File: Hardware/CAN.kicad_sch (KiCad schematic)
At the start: 10 parts, among them J4 Conn_01x02_Pin, U6 TCAN337, U7 CDSOT23-T24CAN

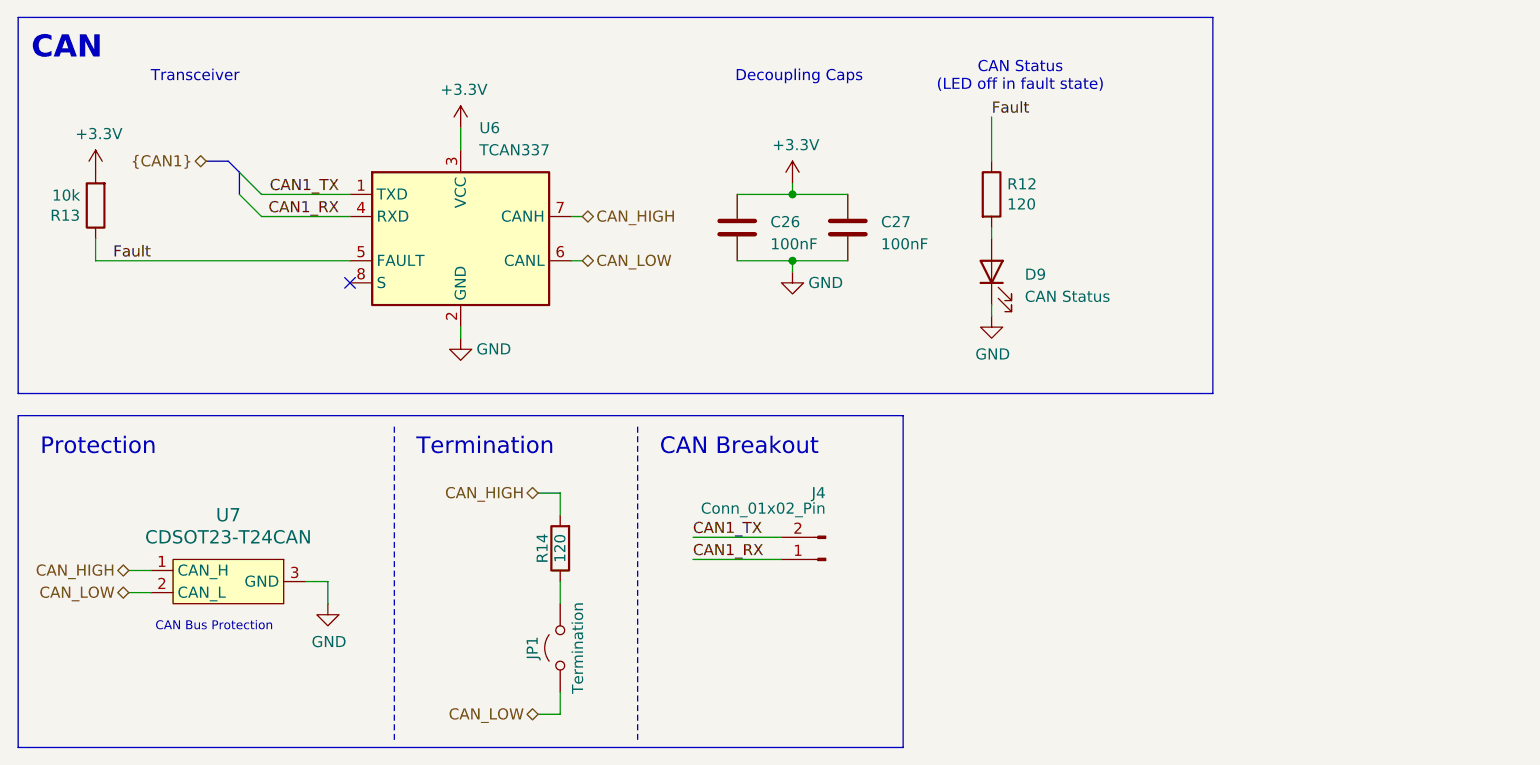
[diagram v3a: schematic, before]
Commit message: changed to 2 channel op amp, stole RPP from PSOM
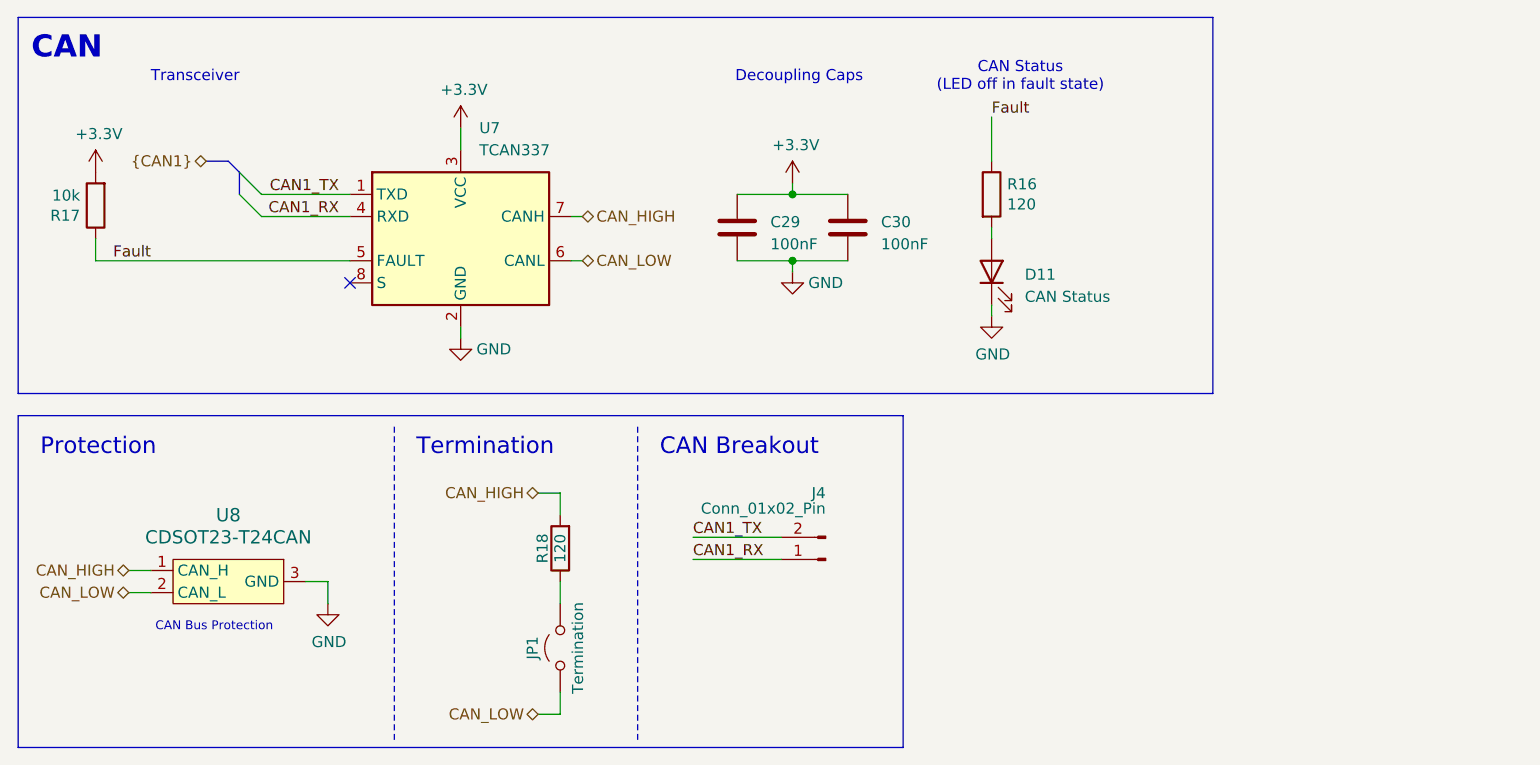
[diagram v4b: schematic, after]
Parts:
- renumbered C26 to C29, C27 to C30, D9 to D11, R12 to R16, R13 to R17, R14 to R18, U6 to U7, U7 to U8
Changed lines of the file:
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@@
 		(on_board yes)
 		(dnp no)
-		(property "Reference" "#PWR062"
+		(property "Reference" "#PWR078"
 			(at 50.8 88.9 0)
 			(effects
@@
 			(project "BPS-AmperesPCB"
 				(path "/a452d214-ea00-440d-a445-5d6103fda43a/2dff07b6-7dab-4ebe-8bad-c03f5c351937"
-					(reference "#PWR062")
+					(reference "#PWR078")
 					(unit 1)
 				)
@@
 		(on_board yes)
 		(dnp no)
-		(property "Reference" "C26"
+		(property "Reference" "C29"
 			(at 101.6 38.735 0)
 			(effects
@@
 			(project "BPS-AmperesPCB"
 				(path "/a452d214-ea00-440d-a445-5d6103fda43a/2dff07b6-7dab-4ebe-8bad-c03f5c351937"
-					(reference "C26")
+					(reference "C29")
 					(unit 1)
 				)
@@
 		(on_board yes)
 		(dnp no)
-		(property "Reference" "R13"
+		(property "Reference" "R17"
 			(at 22.352 37.9984 0)
 			(effects
@@
 			(project "BPS-AmperesPCB"
 				(path "/a452d214-ea00-440d-a445-5d6103fda43a/2dff07b6-7dab-4ebe-8bad-c03f5c351937"
-					(reference "R13")
+					(reference "R17")
 					(unit 1)
 				)
@@
 		(on_board yes)
 		(dnp no)
-		(property "Reference" "R14"
+		(property "Reference" "R18"
 			(at 75.438 76.2 90)
 			(effects
@@
 			(project "BPS-AmperesPCB"
 				(path "/a452d214-ea00-440d-a445-5d6103fda43a/2dff07b6-7dab-4ebe-8bad-c03f5c351937"
-					(reference "R14")
+					(reference "R18")
 					(unit 1)
 				)
@@
 		(on_board yes)
 		(dnp no)
-		(property "Reference" "#PWR060"
+		(property "Reference" "#PWR076"
 			(at 127 55.88 0)
 			(effects
@@
 			(project "BPS-AmperesPCB"
 				(path "/a452d214-ea00-440d-a445-5d6103fda43a/2dff07b6-7dab-4ebe-8bad-c03f5c351937"
-					(reference "#PWR060")
+					(reference "#PWR076")
 					(unit 1)
 				)
@@
 		(on_board yes)
 		(dnp no)
-		(property "Reference" "U7"
+		(property "Reference" "U8"
 			(at 39.37 72.39 0)
 			(effects
@@
 			(project "BPS-AmperesPCB"
 				(path "/a452d214-ea00-440d-a445-5d6103fda43a/2dff07b6-7dab-4ebe-8bad-c03f5c351937"
-					(reference "U7")
+					(reference "U8")
 					(unit 1)
 				)
@@
 		(dnp no)
 		(fields_autoplaced yes)
-		(property "Reference" "D9"
+		(property "Reference" "D11"
 			(at 130.81 44.7674 90)
 			(effects
@@
 			(project ""
 				(path "/a452d214-ea00-440d-a445-5d6103fda43a/2dff07b6-7dab-4ebe-8bad-c03f5c351937"
-					(reference "D9")
+					(reference "D11")
 					(unit 1)
 				)
@@
 		(on_board yes)
 		(dnp no)
-		(property "Reference" "#PWR057"
+		(property "Reference" "#PWR073"
 			(at 24.13 36.83 0)
 			(effects
@@
 			(project "BPS-AmperesPCB"
 				(path "/a452d214-ea00-440d-a445-5d6103fda43a/2dff07b6-7dab-4ebe-8bad-c03f5c351937"
-					(reference "#PWR057")
+					(reference "#PWR073")
 					(unit 1)
 				)
@@
 		(dnp no)
 		(fields_autoplaced yes)
-		(property "Reference" "C27"
+		(property "Reference" "C30"
 			(at 114.3 38.735 0)
 			(effects
@@
 			(project "BPS-AmperesPCB"
 				(path "/a452d214-ea00-440d-a445-5d6103fda43a/2dff07b6-7dab-4ebe-8bad-c03f5c351937"
-					(reference "C27")
+					(reference "C30")
 					(unit 1)
 				)
@@
 		(dnp no)
 		(fields_autoplaced yes)
-		(property "Reference" "U6"
+		(property "Reference" "U7"
 			(at 68.1833 27.94 0)
 			(effects
@@
 			(project "BPS-AmperesPCB"
 				(path "/a452d214-ea00-440d-a445-5d6103fda43a/2dff07b6-7dab-4ebe-8bad-c03f5c351937"
-					(reference "U6")
+					(reference "U7")
 					(unit 1)
 				)
@@
 		(on_board yes)
 		(dnp no)
-		(property "Reference" "#PWR056"
+		(property "Reference" "#PWR072"
 			(at 66.04 31.75 0)
 			(effects
@@
 			(project "BPS-AmperesPCB"
 				(path "/a452d214-ea00-440d-a445-5d6103fda43a/2dff07b6-7dab-4ebe-8bad-c03f5c351937"
-					(reference "#PWR056")
+					(reference "#PWR072")
 					(unit 1)
 				)
@@
 		(on_board yes)
 		(dnp no)
-		(property "Reference" "#PWR059"
+		(property "Reference" "#PWR075"
 			(at 104.14 50.8 0)
 			(effects
@@
 			(project "BPS-AmperesPCB"
 				(path "/a452d214-ea00-440d-a445-5d6103fda43a/2dff07b6-7dab-4ebe-8bad-c03f5c351937"
-					(reference "#PWR059")
+					(reference "#PWR075")
 					(unit 1)
 				)
@@
 		(on_board yes)
 		(dnp no)
-		(property "Reference" "#PWR061"
+		(property "Reference" "#PWR077"
 			(at 66.04 58.42 0)
 			(effects
@@
 			(project "BPS-AmperesPCB"
 				(path "/a452d214-ea00-440d-a445-5d6103fda43a/2dff07b6-7dab-4ebe-8bad-c03f5c351937"
-					(reference "#PWR061")
+					(reference "#PWR077")
 					(unit 1)
 				)
@@
 		(on_board yes)
 		(dnp no)
-		(property "Reference" "#PWR058"
+		(property "Reference" "#PWR074"
 			(at 104.14 38.1 0)
 			(effects
@@
 			(project "BPS-AmperesPCB"
 				(path "/a452d214-ea00-440d-a445-5d6103fda43a/2dff07b6-7dab-4ebe-8bad-c03f5c351937"
-					(reference "#PWR058")
+					(reference "#PWR074")
 					(unit 1)
 				)
@@
 		(on_board yes)
 		(dnp no)
-		(property "Reference" "R12"
+		(property "Reference" "R16"
 			(at 128.778 34.3916 0)
 			(effects
@@
 			(project "BPS-AmperesPCB"
 				(path "/a452d214-ea00-440d-a445-5d6103fda43a/2dff07b6-7dab-4ebe-8bad-c03f5c351937"
-					(reference "R12")
-					(unit 1)
-				)
+					(reference "R16")
+					(unit 1)
+				)

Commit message: lay out lay out
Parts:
- renumbered C29 to C30, C30 to C31, D11 to D12, U7 to U6, U8 to U7
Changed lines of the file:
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@@
 		(on_board yes)
 		(dnp no)
-		(property "Reference" "#PWR079"
+		(property "Reference" "#PWR081"
 			(at 50.8 88.9 0)
 			(effects
@@
 			(project "BPS-AmperesPCB"
 				(path "/a452d214-ea00-440d-a445-5d6103fda43a/2dff07b6-7dab-4ebe-8bad-c03f5c351937"
-					(reference "#PWR079")
+					(reference "#PWR081")
 					(unit 1)
 				)
@@
 		(on_board yes)
 		(dnp no)
-		(property "Reference" "C29"
+		(property "Reference" "C30"
 			(at 101.6 38.735 0)
 			(effects
@@
 			(project "BPS-AmperesPCB"
 				(path "/a452d214-ea00-440d-a445-5d6103fda43a/2dff07b6-7dab-4ebe-8bad-c03f5c351937"
-					(reference "C29")
+					(reference "C30")
 					(unit 1)
 				)
@@
 		(on_board yes)
 		(dnp no)
-		(property "Reference" "#PWR077"
+		(property "Reference" "#PWR079"
 			(at 127 55.88 0)
 			(effects
@@
 			(project "BPS-AmperesPCB"
 				(path "/a452d214-ea00-440d-a445-5d6103fda43a/2dff07b6-7dab-4ebe-8bad-c03f5c351937"
-					(reference "#PWR077")
+					(reference "#PWR079")
 					(unit 1)
 				)
@@
 		(on_board yes)
 		(dnp no)
-		(property "Reference" "U8"
+		(property "Reference" "U7"
 			(at 39.37 72.39 0)
 			(effects
@@
 			(project "BPS-AmperesPCB"
 				(path "/a452d214-ea00-440d-a445-5d6103fda43a/2dff07b6-7dab-4ebe-8bad-c03f5c351937"
-					(reference "U8")
+					(reference "U7")
 					(unit 1)
 				)
@@
 		(dnp no)
 		(fields_autoplaced yes)
-		(property "Reference" "D11"
+		(property "Reference" "D12"
 			(at 130.81 44.7674 90)
 			(effects
@@
 			(project ""
 				(path "/a452d214-ea00-440d-a445-5d6103fda43a/2dff07b6-7dab-4ebe-8bad-c03f5c351937"
-					(reference "D11")
+					(reference "D12")
 					(unit 1)
 				)
@@
 		(on_board yes)
 		(dnp no)
-		(property "Reference" "#PWR074"
+		(property "Reference" "#PWR076"
 			(at 24.13 36.83 0)
 			(effects
@@
 			(project "BPS-AmperesPCB"
 				(path "/a452d214-ea00-440d-a445-5d6103fda43a/2dff07b6-7dab-4ebe-8bad-c03f5c351937"
-					(reference "#PWR074")
+					(reference "#PWR076")
 					(unit 1)
 				)
@@
 		(dnp no)
 		(fields_autoplaced yes)
-		(property "Reference" "C30"
+		(property "Reference" "C31"
 			(at 114.3 38.735 0)
 			(effects
@@
 			(project "BPS-AmperesPCB"
 				(path "/a452d214-ea00-440d-a445-5d6103fda43a/2dff07b6-7dab-4ebe-8bad-c03f5c351937"
-					(reference "C30")
+					(reference "C31")
 					(unit 1)
 				)
@@
 		(dnp no)
 		(fields_autoplaced yes)
-		(property "Reference" "U7"
+		(property "Reference" "U6"
 			(at 68.1833 27.94 0)
 			(effects
@@
 			(project "BPS-AmperesPCB"
 				(path "/a452d214-ea00-440d-a445-5d6103fda43a/2dff07b6-7dab-4ebe-8bad-c03f5c351937"
-					(reference "U7")
+					(reference "U6")
 					(unit 1)
 				)
@@
 		(on_board yes)
 		(dnp no)
-		(property "Reference" "#PWR073"
+		(property "Reference" "#PWR075"
 			(at 66.04 31.75 0)
 			(effects
@@
 			(project "BPS-AmperesPCB"
 				(path "/a452d214-ea00-440d-a445-5d6103fda43a/2dff07b6-7dab-4ebe-8bad-c03f5c351937"
-					(reference "#PWR073")
+					(reference "#PWR075")
 					(unit 1)
 				)
@@
 		(on_board yes)
 		(dnp no)
-		(property "Reference" "#PWR076"
+		(property "Reference" "#PWR078"
 			(at 104.14 50.8 0)
 			(effects
@@
 			(project "BPS-AmperesPCB"
 				(path "/a452d214-ea00-440d-a445-5d6103fda43a/2dff07b6-7dab-4ebe-8bad-c03f5c351937"
-					(reference "#PWR076")
+					(reference "#PWR078")
 					(unit 1)
 				)
@@
 		(on_board yes)
 		(dnp no)
-		(property "Reference" "#PWR078"
+		(property "Reference" "#PWR080"
 			(at 66.04 58.42 0)
 			(effects
@@
 			(project "BPS-AmperesPCB"
 				(path "/a452d214-ea00-440d-a445-5d6103fda43a/2dff07b6-7dab-4ebe-8bad-c03f5c351937"
-					(reference "#PWR078")
+					(reference "#PWR080")
 					(unit 1)
 				)
@@
 		(on_board yes)
 		(dnp no)
-		(property "Reference" "#PWR075"
+		(property "Reference" "#PWR077"
 			(at 104.14 38.1 0)
 			(effects
@@
 			(project "BPS-AmperesPCB"
 				(path "/a452d214-ea00-440d-a445-5d6103fda43a/2dff07b6-7dab-4ebe-8bad-c03f5c351937"
-					(reference "#PWR075")
-					(unit 1)
-				)
+					(reference "#PWR077")
+					(unit 1)
+				)

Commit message: updated some component part nums
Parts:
- C30, C31: Mfg (none) -> MLASH168SB7104KTNA01; P/N C0805C104M5RACTU -> MLASH168SB7104KTNA01
- R16: Mfg (none) -> CRCW0603120RFKEC; P/N SDR10EZPF2200 -> CRCW0603120RFKEC
- R17: Mfg (none) -> CRCW060310K0FKEI; P/N CRCW08054K70FKEA -> CRCW060310K0FKEI
- R18: Mfg (none) -> CRCW0603120RFKEC; P/N CRCW080559R0FKEA -> CRCW0603120RFKEC
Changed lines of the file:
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@@
 			)
 		)
-		(property "P/N" "C0805C104M5RACTU"
+		(property "P/N" "MLASH168SB7104KTNA01"
+			(at 97.79 39.37 0)
+			(effects
+				(font
+					(size 1.27 1.27)
+				)
+				(hide yes)
+			)
+		)
+		(property "Mfg" "MLASH168SB7104KTNA01"
 			(at 97.79 39.37 0)
 			(effects
@@
 			)
 		)
-		(property "P/N" "CRCW08054K70FKEA"
+		(property "P/N" "CRCW060310K0FKEI "
+			(at 24.13 36.83 0)
+			(effects
+				(font
+					(size 1.27 1.27)
+				)
+				(hide yes)
+			)
+		)
+		(property "Mfg" "CRCW060310K0FKEI "
 			(at 24.13 36.83 0)
 			(effects
@@
 			)
 		)
-		(property "P/N" "CRCW080559R0FKEA"
+		(property "P/N" "CRCW0603120RFKEC "
 			(at 77.47 76.2 0)
 			(effects
@@
 		(property "p/n" ""
 			(at 77.47 76.2 0)
+			(effects
+				(font
+					(size 1.27 1.27)
+				)
+				(hide yes)
+			)
+		)
+		(property "Mfg" "CRCW0603120RFKEC "
+			(at 77.47 76.2 90)
 			(effects
 				(font
@@
 			)
 		)
-		(property "P/N" "C0805C104M5RACTU"
+		(property "P/N" "MLASH168SB7104KTNA01"
+			(at 110.49 39.37 0)
+			(effects
+				(font
+					(size 1.27 1.27)
+				)
+				(hide yes)
+			)
+		)
+		(property "Mfg" "MLASH168SB7104KTNA01"
 			(at 110.49 39.37 0)
 			(effects
@@
 			)
 		)
-		(property "P/N" "SDR10EZPF2200"
+		(property "P/N" "CRCW0603120RFKEC "
 			(at 127 35.56 0)
 			(effects
@@
 			(at 127 35.56 0)
 			(effects
+				(font
+					(size 1.27 1.27)
+				)
+				(hide yes)
+			)
+		)
+		(property "Mfg" "CRCW0603120RFKEC "
+			(at 127 35.56 0)
+			(effects

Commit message: generated production stuff
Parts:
- D12: Mfg (none) -> XL-1608UBC-06A; P/N (none) -> XL-1608UBC-06A
- J4: P/N (none) -> 1053091202
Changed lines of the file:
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@@
+			)
+		)
+		(property "P/N" "1053091202"
+			(at 107.95 77.47 0)
+			(effects
+				(font
+					(size 1.27 1.27)
+				)
+				(hide yes)
 			)
 		)
@@
 			(effects
 				(font
+					(size 1.27 1.27)
+				)
+				(hide yes)
+			)
+		)
+		(property "Mfg" "XL-1608UBC-06A"
+			(at 127 44.45 90)
+			(effects
+				(font
+					(size 1.27 1.27)
+				)
+				(hide yes)
+			)
+		)
+		(property "P/N" "XL-1608UBC-06A"
+			(at 127 44.45 90)
+			(effects
+				(font
